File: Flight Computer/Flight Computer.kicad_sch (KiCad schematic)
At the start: 1 part, among them IC1 ESP32-Wrover-IE-N16R8

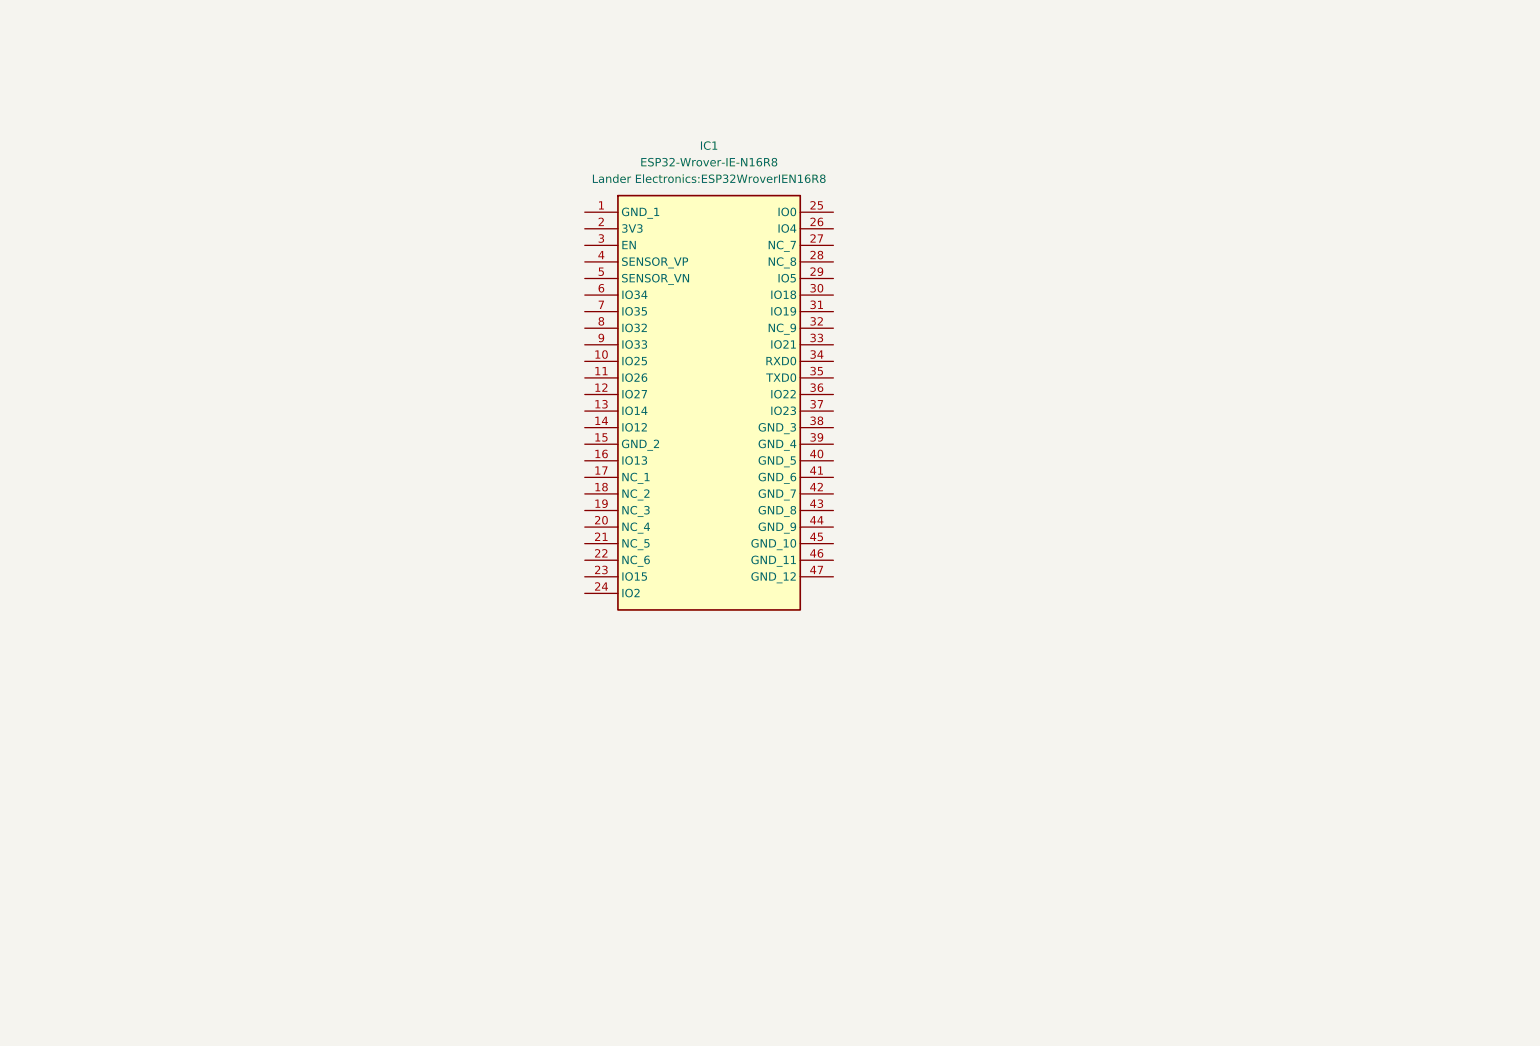
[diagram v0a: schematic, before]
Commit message: Added barometric pressure sensors and IMUs to footprint and symbol library
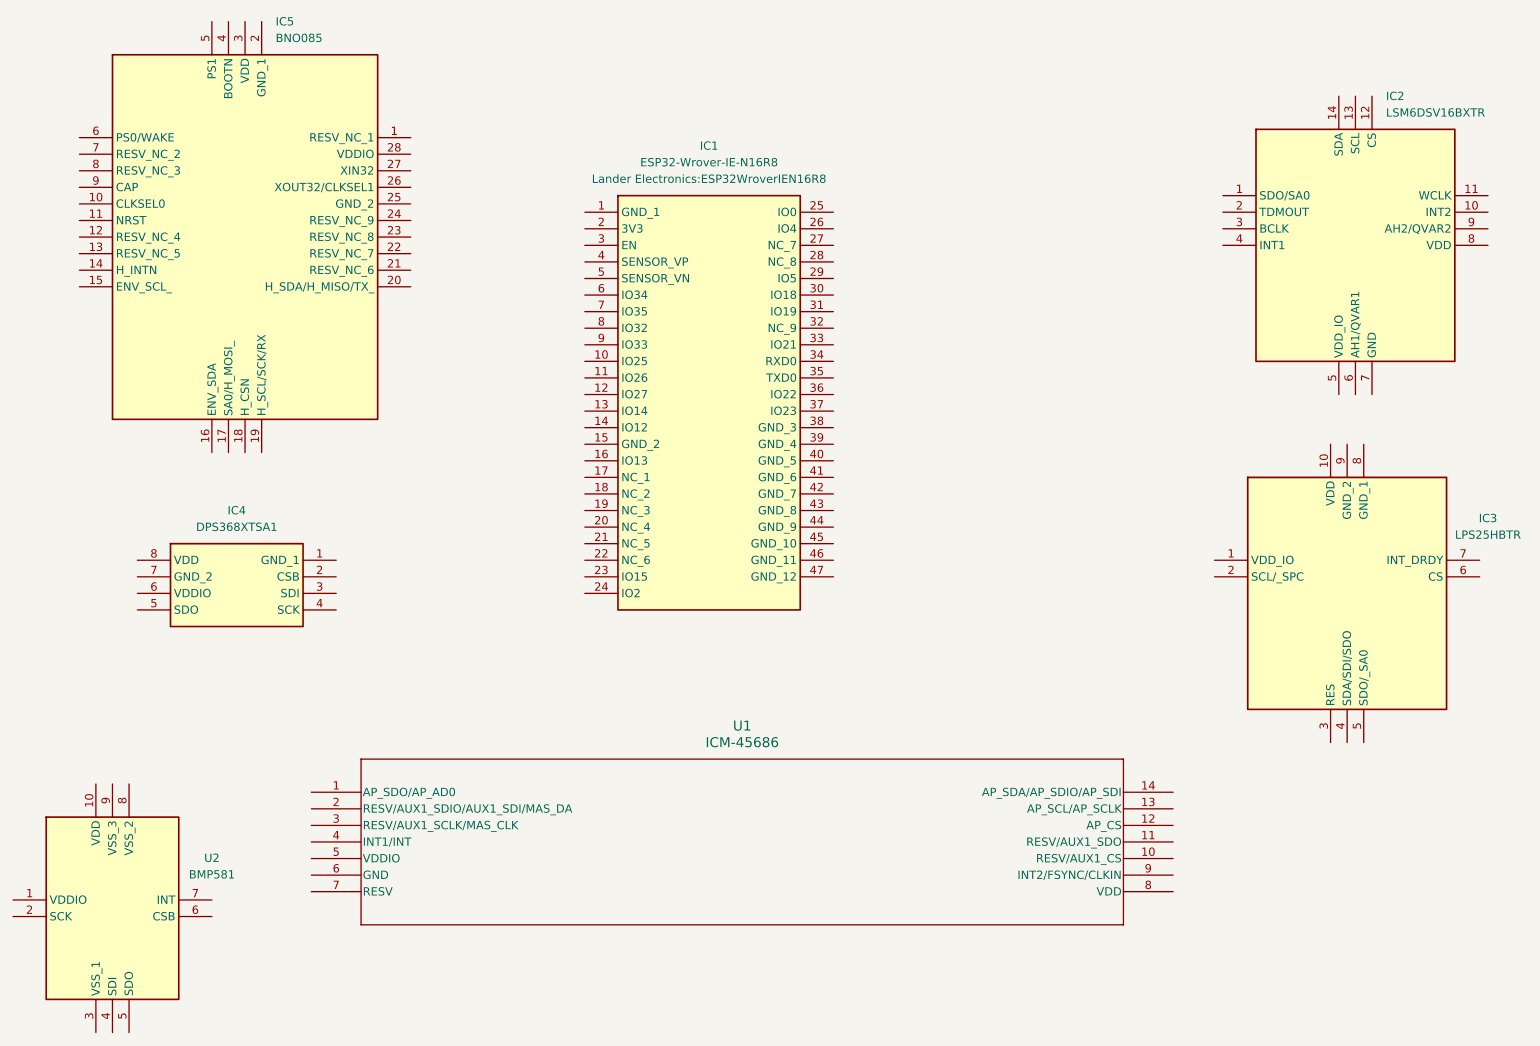
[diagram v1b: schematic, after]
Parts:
- added IC2: LSM6DSV16BXTR, Lander Electronics:LSM6DSV16BXTR, symbol Lander Electronics:LSM6DSV16BXTR
- added IC3: LPS25HBTR, Lander Electronics:LPS25HBTR, symbol Lander Electronics:LPS25HBTR
- added IC4: DPS368XTSA1, Lander Electronics:DPS368XTSA1, symbol Lander Electronics:DPS368XTSA1
- added IC5: BNO085, Lander Electronics:BNO085, symbol Lander Electronics:BNO085
- added U1: ICM-45686, Lander Electronics:ICM45686, symbol Lander Electronics:ICM-45686
- added U2: BMP581, Lander Electronics:BMP581, symbol Lander Electronics:BMP581

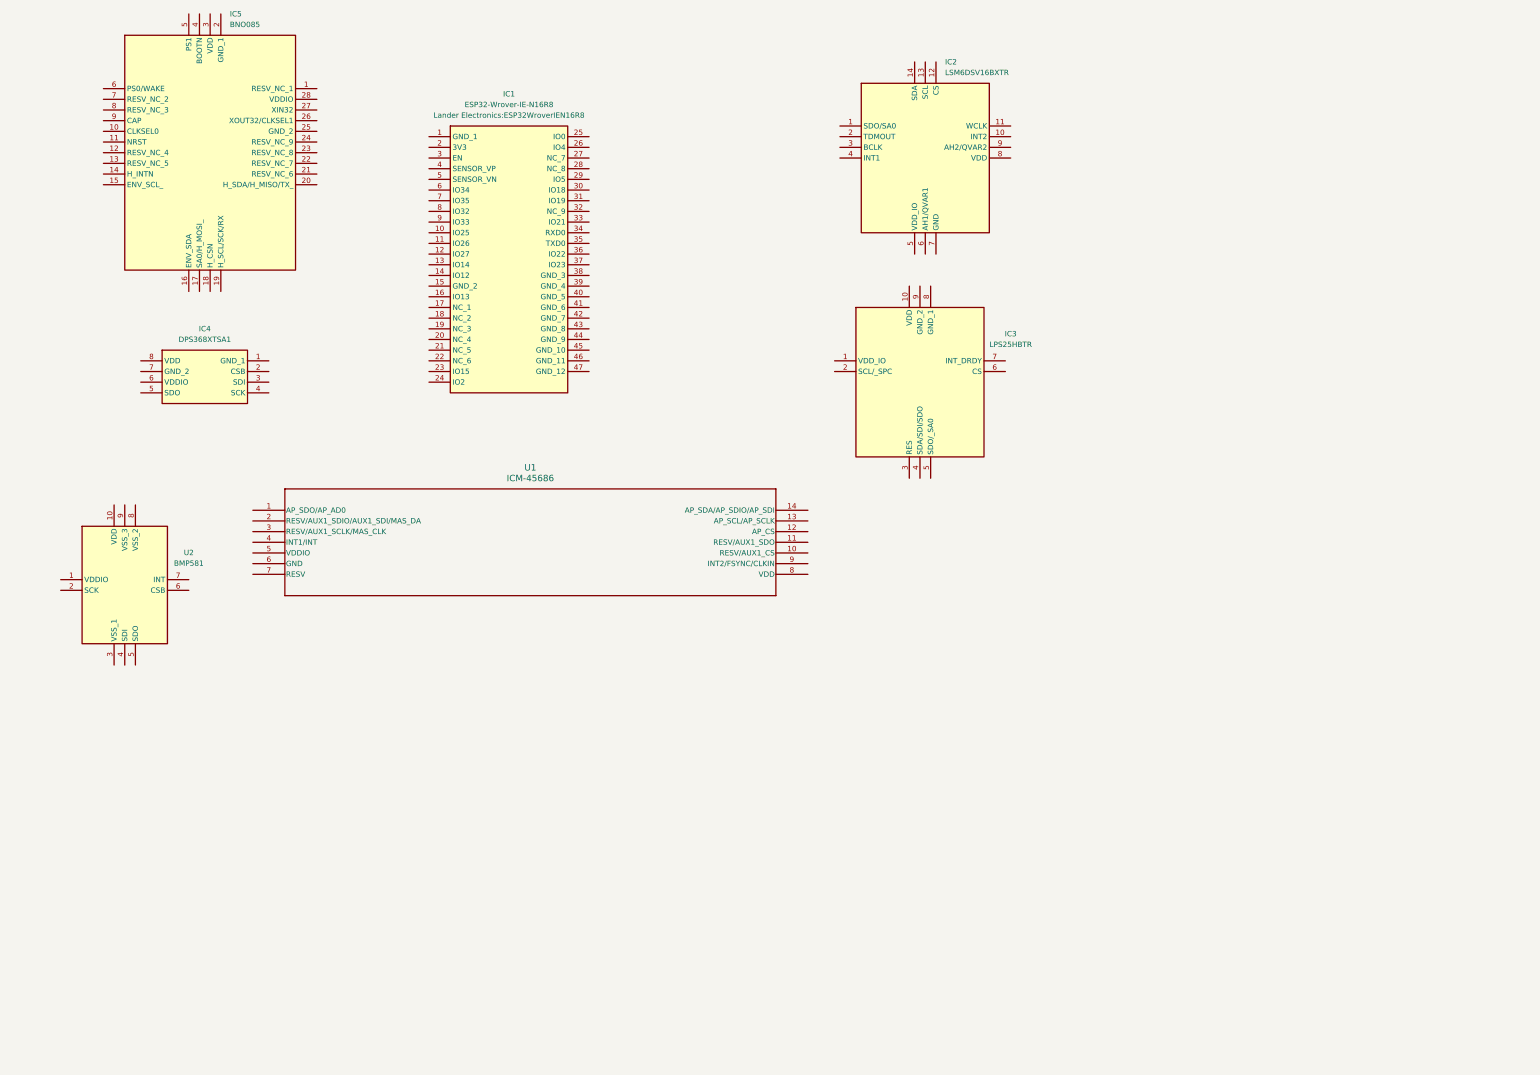
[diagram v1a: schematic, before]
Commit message: Integrate Sensor for Flight Computer
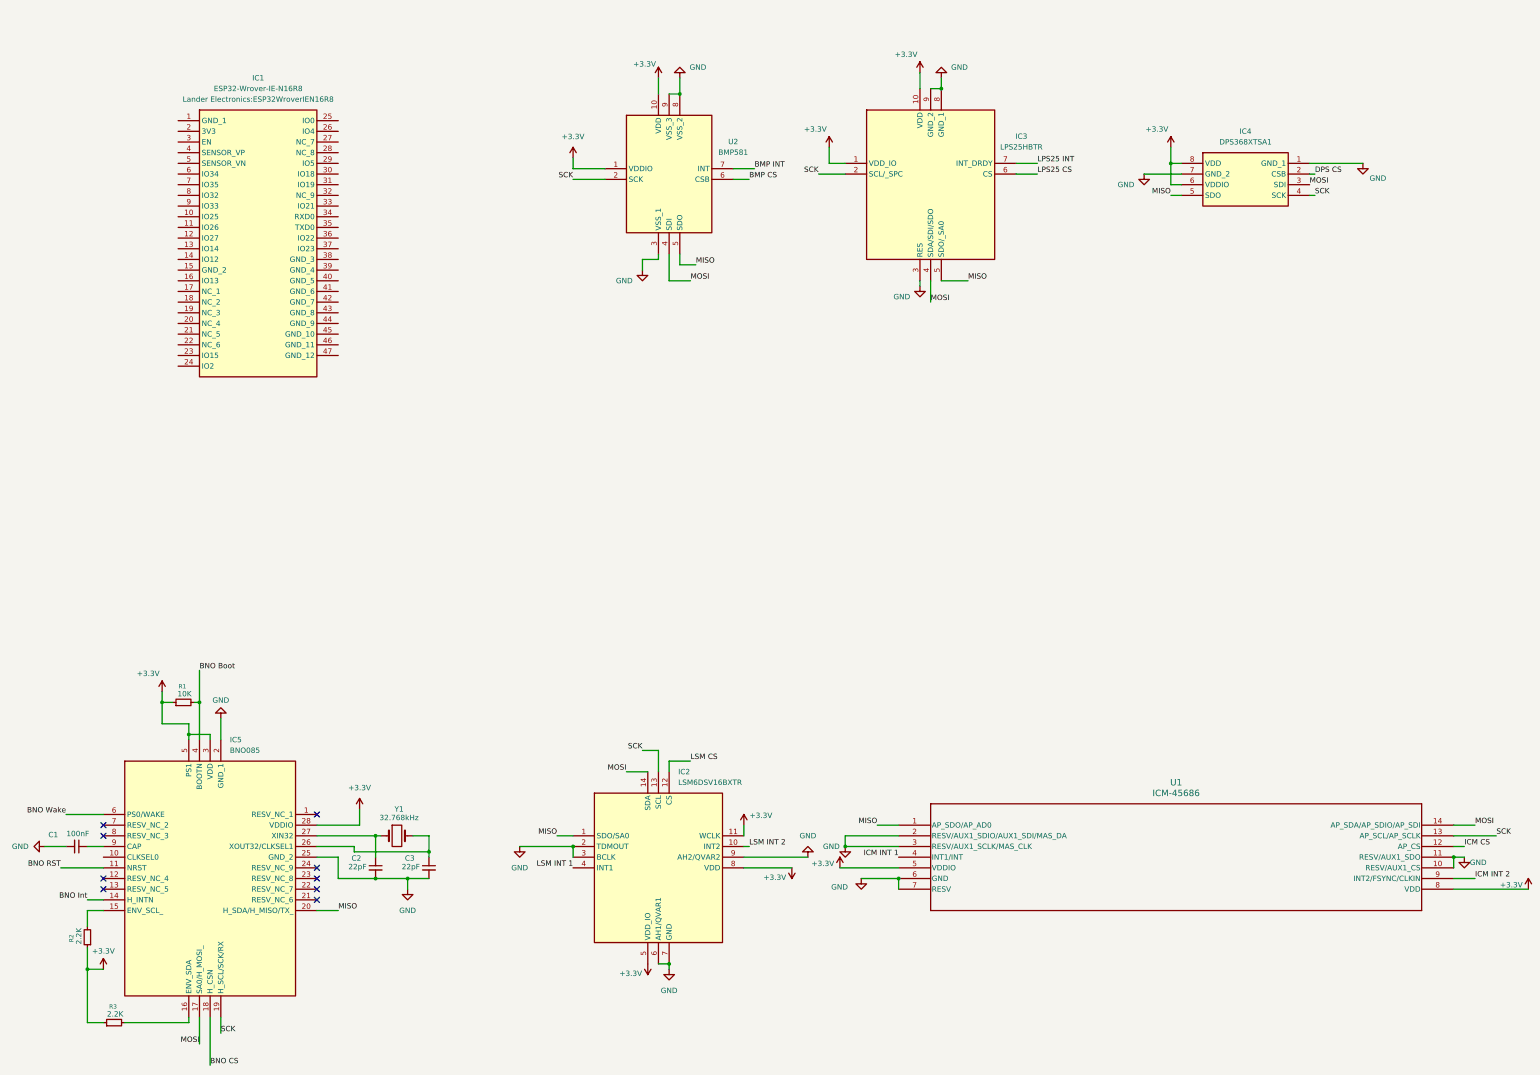
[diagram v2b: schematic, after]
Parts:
- added C1: 100nF, symbol Device:C_Small
- added C2, C3: 22pF, symbol Device:C_Small
- added R1: 10K, symbol Device:R_Small
- added R2, R3: 2.2K, symbol Device:R_Small
- added Y1: 32.768kHz, symbol Device:Crystal
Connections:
- net +3.3V: now reaches IC3.1 (VDD_IO)
- net +3.3V: now also IC2.11 (WCLK), IC2.5 (VDD_IO), IC2.8 (VDD), IC3.10 (VDD), IC4.6 (VDDIO), IC4.8 (VDD), IC5.28 (VDDIO), IC5.3 (VDD), IC5.5 (PS1), U1.5 (VDDIO), U1.8 (VDD), U2.1 (VDDIO), U2.10 (VDD), R1.1, R2.1, R3.1
- net SCK: now reaches IC3.2 (SCL/_SPC)
- net SCK: now also IC2.13 (SCL), IC4.4 (SCK), IC5.19 (H_SCL/SCK/RX), U1.13 (AP_SCL/AP_SCLK), U2.2 (SCK)
- net GND: now reaches IC3.3 (RES)
- net GND: now also IC2.2 (TDMOUT), IC2.3 (BCLK), IC2.6 (AH1/QVAR1), IC2.7 (GND), IC2.9 (AH2/QVAR2), IC3.8 (GND_1), IC3.9 (GND_2), IC4.1 (GND_1), IC4.7 (GND_2), IC5.2 (GND_1), IC5.25 (GND_2), U1.10 (RESV/AUX1_CS), U1.11 (RESV/AUX1_SDO), U1.2 (RESV/AUX1_SDIO/AUX1_SDI/MAS_DA), U1.3 (RESV/AUX1_SCLK/MAS_CLK), U1.6 (GND), U1.7 (RESV), U2.3 (VSS_1), U2.8 (VSS_2), U2.9 (VSS_3), C1.2, C2.2, C3.2
- net MOSI: now reaches IC3.4 (SDA/SDI/SDO)
- net MOSI: now also IC2.14 (SDA), IC4.3 (SDI), IC5.17 (SA0/H_MOSI_), U1.14 (AP_SDA/AP_SDIO/AP_SDI), U2.4 (SDI)
- net MISO: now reaches IC3.5 (SDO/_SA0)
- net MISO: now also IC2.1 (SDO/SA0), IC4.5 (SDO), IC5.20 (H_SDA/H_MISO/TX_), U1.1 (AP_SDO/AP_AD0), U2.5 (SDO)
- net LPS25 CS: now reaches IC3.6 (CS)
- net LPS25 INT: now reaches IC3.7 (INT_DRDY)
- net BMP CS: now reaches U2.6 (CSB)
- net BMP INT: now reaches U2.7 (INT)
- net ICM CS: now reaches U1.12 (AP_CS)
- net ICM INT 1: now reaches U1.4 (INT1/INT)
- net ICM INT 2: now reaches U1.9 (INT2/FSYNC/CLKIN)
- net DPS CS: now reaches IC4.2 (CSB)
- net LSM INT 2: now reaches IC2.10 (INT2)
- net LSM CS: now reaches IC2.12 (CS)
- net LSM INT 1: now reaches IC2.4 (INT1)
- net BNO RST: now reaches IC5.11 (NRST)
- net BNO Int: now reaches IC5.14 (H_INTN)
- net at IC5.15 (ENV_SCL_): now also R2.2
- net at IC5.16 (ENV_SDA): now also R3.2
- net BNO CS: now reaches IC5.18 (H_CSN)
- net at IC5.26 (XOUT32/CLKSEL1): now also C3.1, Y1.2
- net at IC5.27 (XIN32): now also C2.1, Y1.1
- net BNO Boot: now reaches IC5.4 (BOOTN)
- net BNO Boot: now also R1.2
- net BNO Wake: now reaches IC5.6 (PS0/WAKE)
- net at IC5.9 (CAP): now also C1.1
- no-connect marks 0 -> 9
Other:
- moved on the sheet: IC1, IC2, IC3, IC4, IC5, U1, U2

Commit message: Use heirarchical sheets for flight computer and add power supply filter capacitors
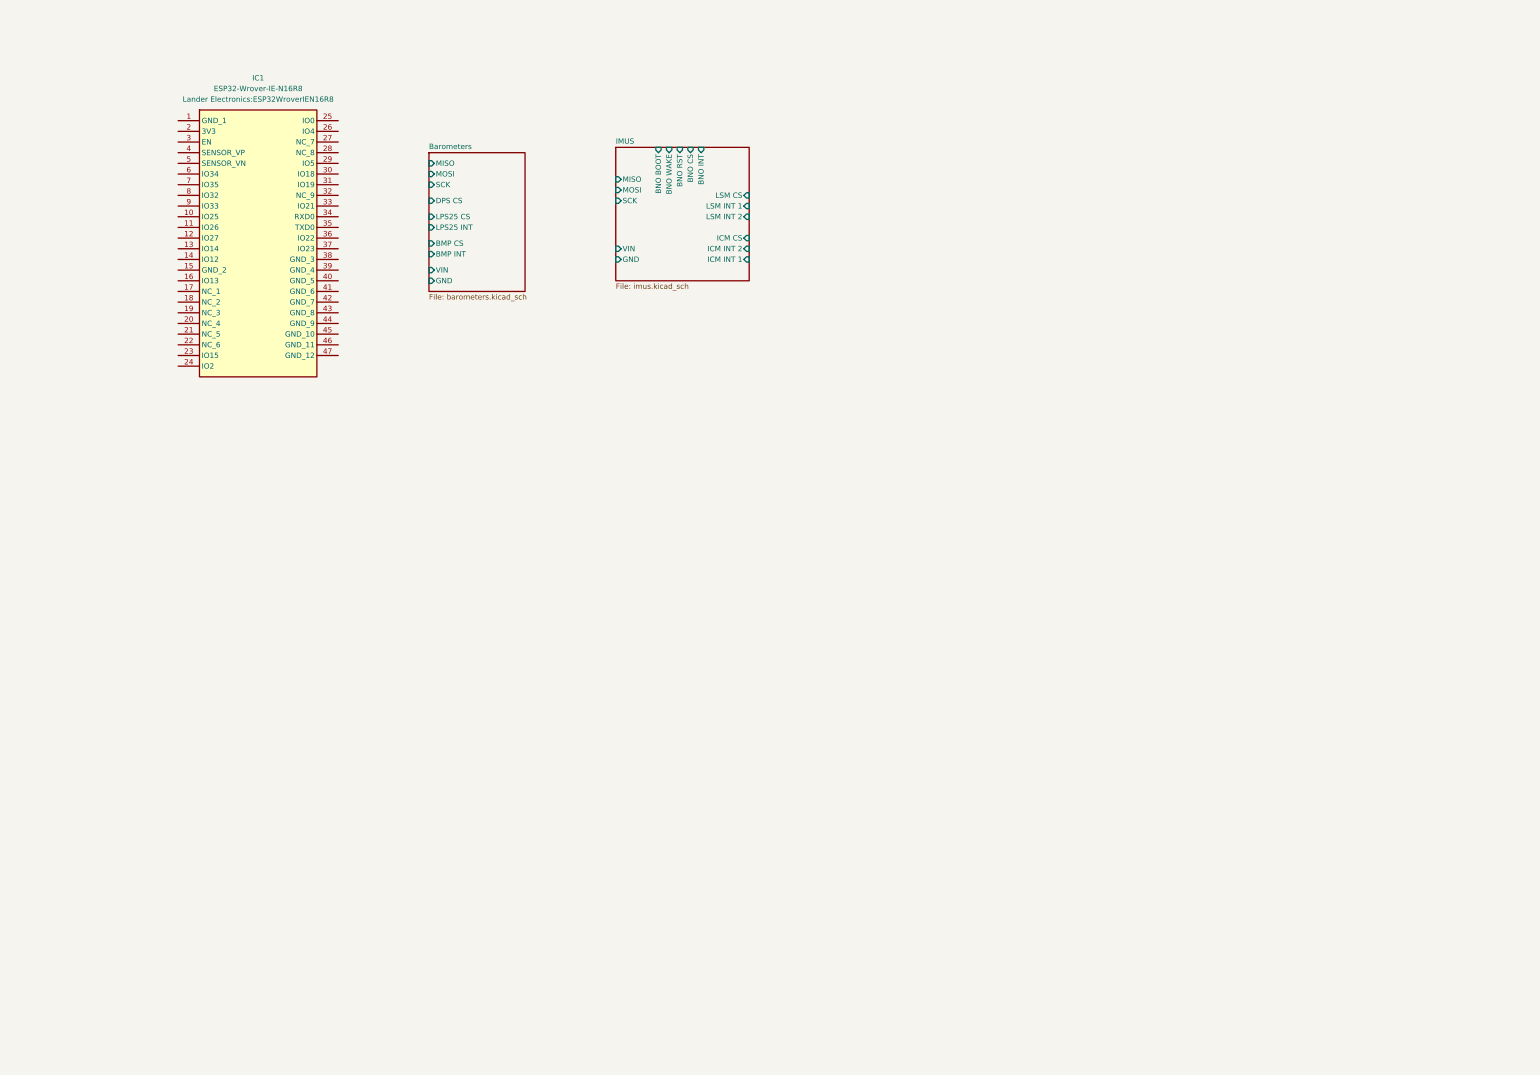
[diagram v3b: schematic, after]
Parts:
- removed C1: 100nF, symbol Device:C_Small
- removed C2, C3: 22pF, symbol Device:C_Small
- removed IC2: LSM6DSV16BXTR, Lander Electronics:LSM6DSV16BXTR, symbol Lander Electronics:LSM6DSV16BXTR
- removed IC3: LPS25HBTR, Lander Electronics:LPS25HBTR, symbol Lander Electronics:LPS25HBTR
- removed IC4: DPS368XTSA1, Lander Electronics:DPS368XTSA1, symbol Lander Electronics:DPS368XTSA1
- removed IC5: BNO085, Lander Electronics:BNO085, symbol Lander Electronics:BNO085
- removed R1: 10K, symbol Device:R_Small
- removed R2, R3: 2.2K, symbol Device:R_Small
- removed U1: ICM-45686, Lander Electronics:ICM45686, symbol Lander Electronics:ICM-45686
- removed U2: BMP581, Lander Electronics:BMP581, symbol Lander Electronics:BMP581
- removed Y1: 32.768kHz, symbol Device:Crystal
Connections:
- no-connect marks 9 -> 0
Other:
- added sheet Barometers (barometers.kicad_sch)
- added sheet IMUS (imus.kicad_sch)
